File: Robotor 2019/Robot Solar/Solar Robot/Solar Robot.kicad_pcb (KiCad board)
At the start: 2 copper layers, 100.3 x 81.3 mm, 43 parts, among them J1 Conn_01x02, J2 Conn_01x06_Male, M1 Motor_DC, M2 Motor_DC, SW1 SW_DIP_x01, SW2 SW_Push, SW3 SW_Push, U1 ATmega328-PU, U2 ITR8307, U3 ITR8307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

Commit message: Solar robot final circuit board (hopefully)
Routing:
- net Net-(R4-Pad2): track 15.7 -> 18.7 mm
- net Net-(R10-Pad2): track 16.3 -> 18.8 mm
- net GND: vias 4 -> 0

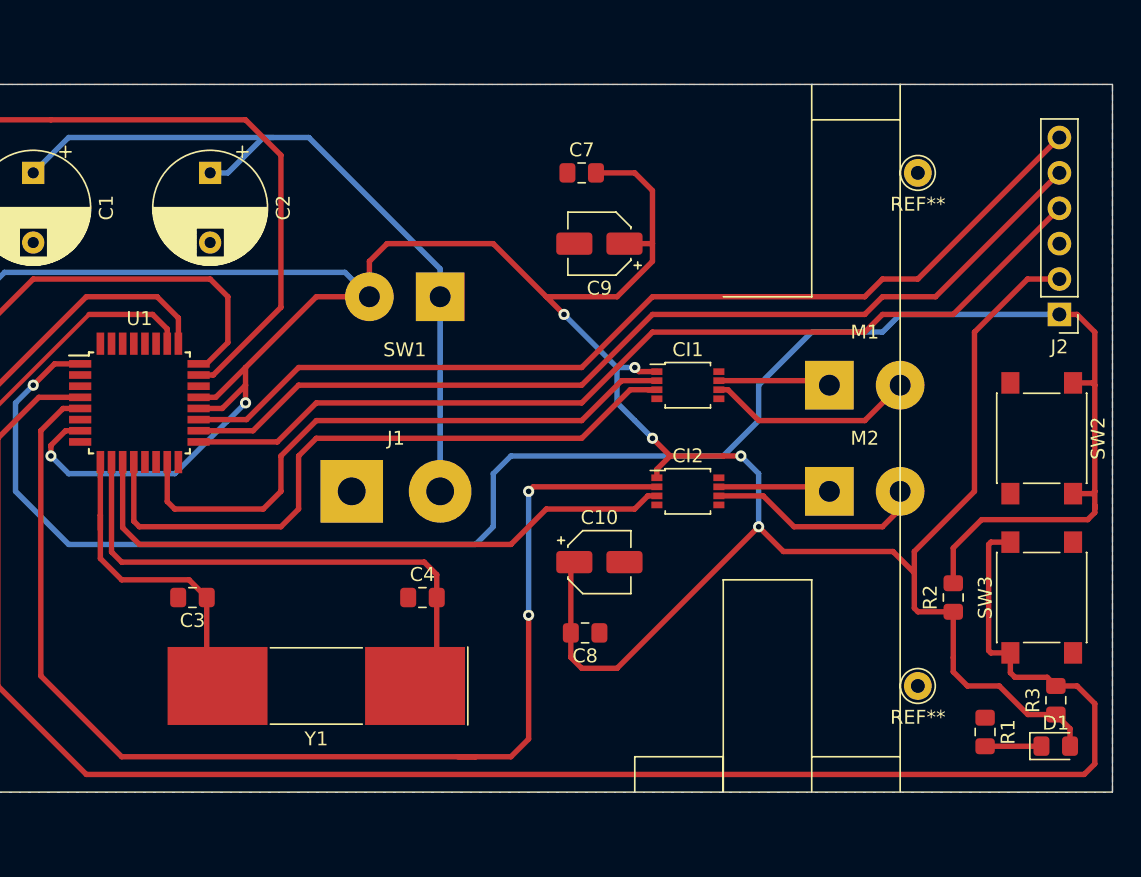
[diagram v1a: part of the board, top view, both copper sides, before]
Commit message: Final solar robot pcb schematic (added mounting holes for motors and changed clearance on existing through-holes) Added all-red pdf printer file.
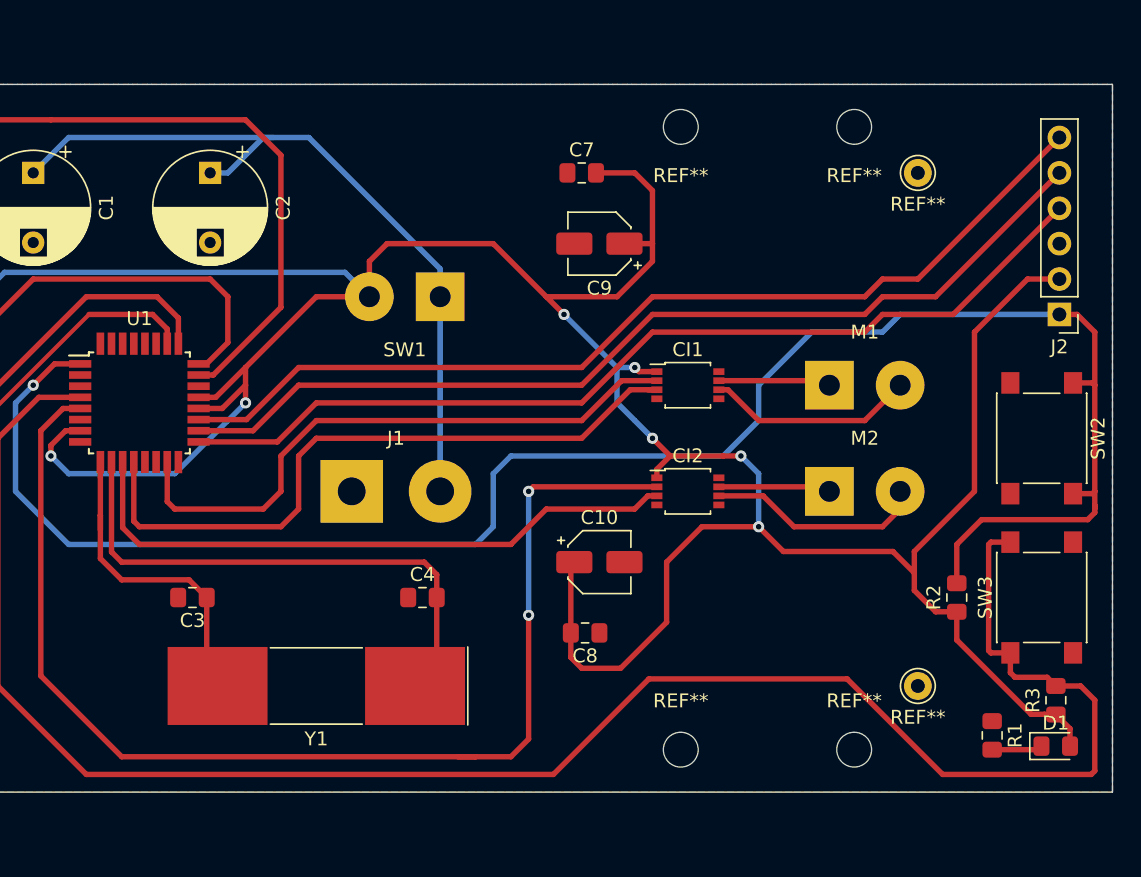
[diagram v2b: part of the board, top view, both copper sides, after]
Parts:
- added REF**: MountingHole_2.5mm, MountingHole:MountingHole_2.5mm, F.Cu at (112.5, 72.9)
- added REF**: MountingHole_2.5mm, MountingHole:MountingHole_2.5mm, F.Cu at (125.0, 72.9)
- added REF**: MountingHole_2.5mm, MountingHole:MountingHole_2.5mm, F.Cu at (112.5, 117.6)
- added REF**: MountingHole_2.5mm, MountingHole:MountingHole_2.5mm, F.Cu at (125.0, 117.6)
- moved R1 0.56 mm to (134.9, 116.6)
- moved R2 0.25 mm to (132.3, 106.7)
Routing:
- net StartBtn: track 130.2 -> 136.3 mm

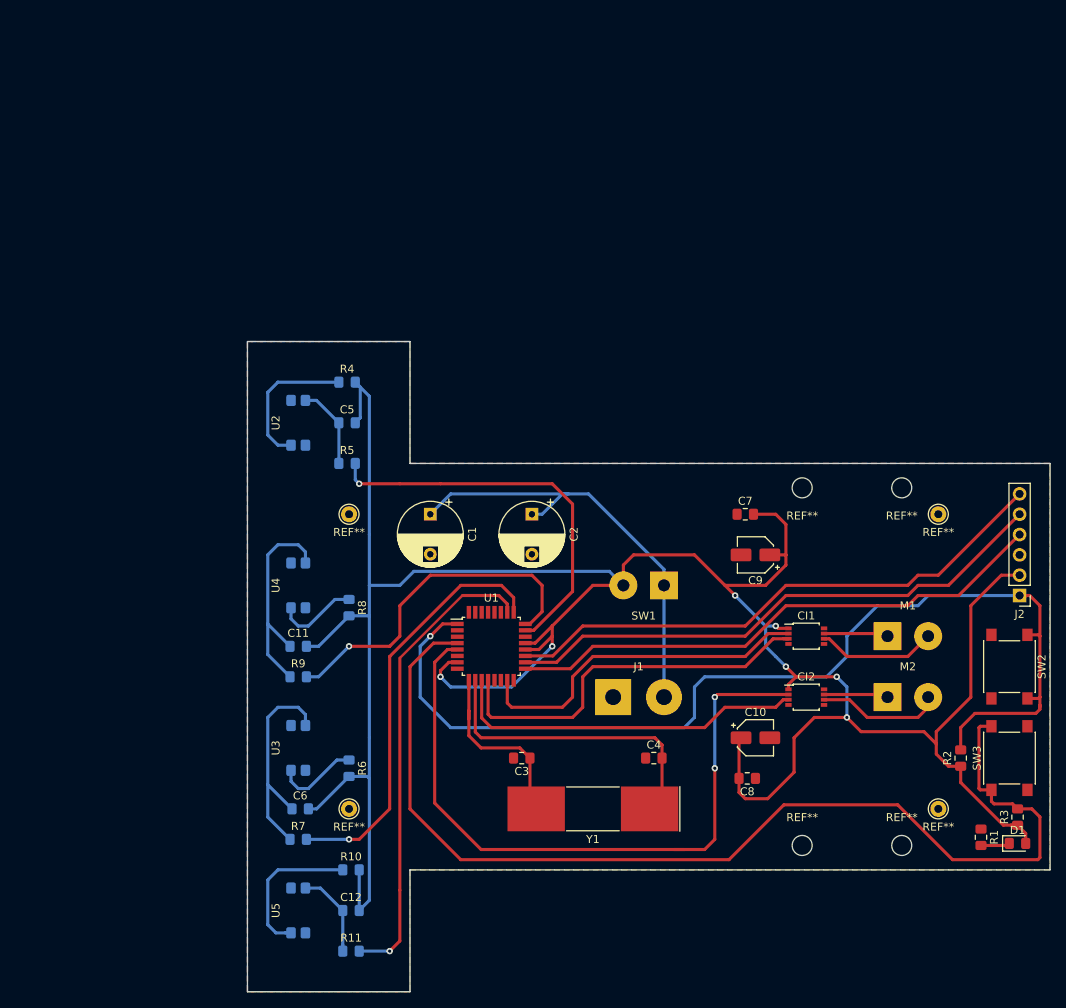
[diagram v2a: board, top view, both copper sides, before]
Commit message: Tweaked PCB track widths. Added compnent values in both eschemas. Printed Front and Back tracks and a parts list to PDF.
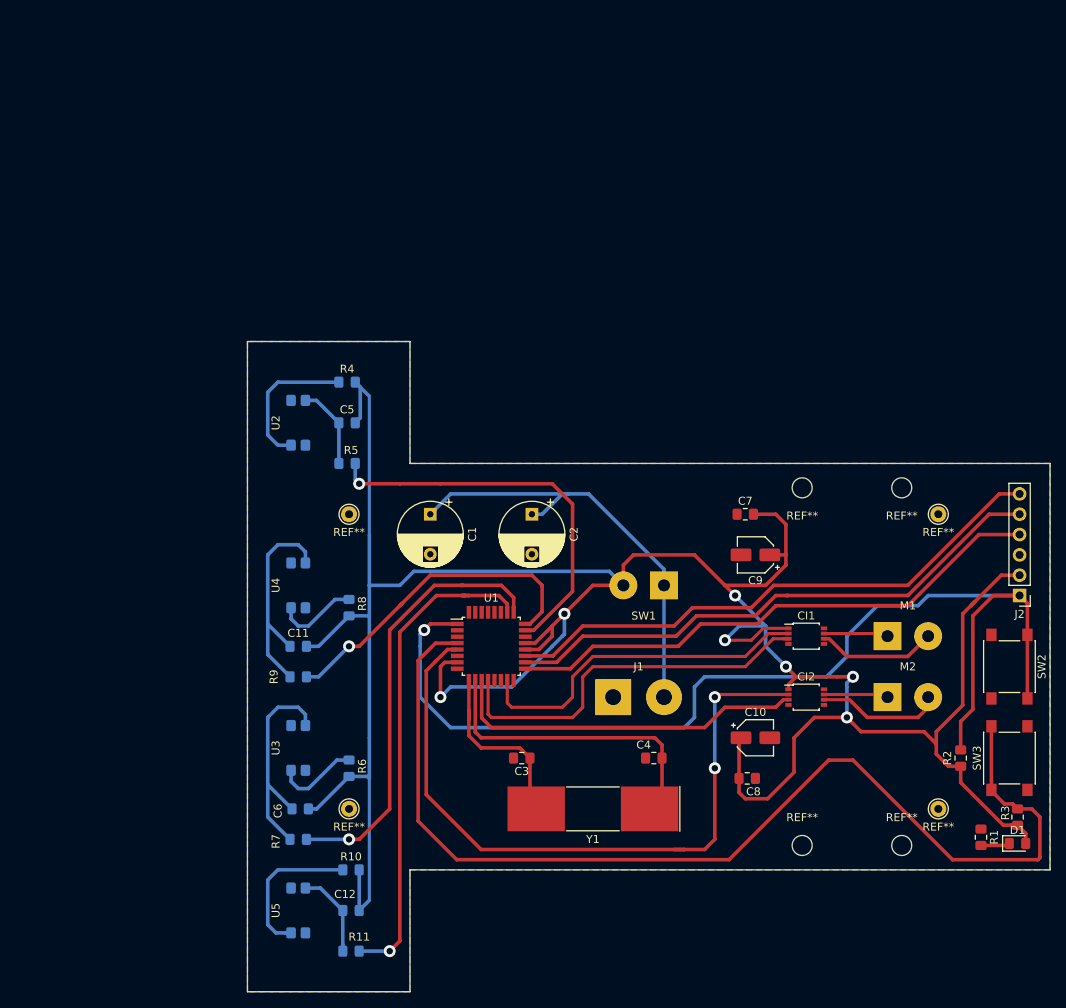
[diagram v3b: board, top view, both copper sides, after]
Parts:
- C1, C2: value CP -> 3F
- C10, C9: value CP -> 10uF
- C11, C12, C5, C6: value C -> 10nF
- C3, C4: value C -> 22p
- C7, C8: value C -> 100n
- Y1: value Crystal -> 16Mhz
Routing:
- net +5V: track 326.0 -> 346.1 mm
- net RESET: track 132.4 -> 137.7 mm
- net S4: track 59.1 -> 62.3 mm
- net S2: track 52.7 -> 54.9 mm
- net S3: track 43.5 -> 41.6 mm
- net M2IN1: track 87.4 -> 88.6 mm

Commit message: no message
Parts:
- added C13: 100n, Capacitor_SMD:C_0805_2012Metric_Pad1.15x1.40mm_HandSolder, F.Cu at (57.3, 41.8)
- added C14: 100n, Capacitor_SMD:C_0805_2012Metric_Pad1.15x1.40mm_HandSolder, F.Cu at (57.6, 36.7)
- added C15: 100n, Capacitor_SMD:C_0805_2012Metric_Pad1.15x1.40mm_HandSolder, F.Cu at (61.6, 36.7)
- U1: value ATmega328-PU -> ATmega328P-AU
- moved Y1 77.6 mm to (32.5, 57.2), turned to 90 degrees
- moved C4 73.3 mm to (37.4, 60.0), turned to 90 degrees
- moved C3 67.4 mm to (37.3, 52.5), turned to 90 degrees
- moved R7 52.4 mm to (17.4, 75.5), turned to 90 degrees
- moved C2 52.0 mm to (46.3, 35.5), turned to 0 degrees
- moved R9 50.9 mm to (19.0, 55.9)
- moved C8 49.9 mm to (76.7, 68.6)
- moved CI2 49.9 mm to (84.1, 58.4)
- moved D1 49.9 mm to (110.5, 76.7)
- moved J1 49.9 mm to (60.0, 58.4)
- moved R2 49.9 mm to (103.4, 66.0)
- moved R6 49.9 mm to (27.0, 67.3)
- moved REF** 49.9 mm to (83.6, 76.9)
- moved REF** 49.9 mm to (96.1, 76.9)
- moved REF** 49.9 mm to (27.0, 72.4)
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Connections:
- U1 pad 1: RESET -> Net-(U1-Pad1)
- U1 pad 10: Net-(C4-Pad2) -> M2IN1
- U1 pad 11: M2IN2 -> Net-(U1-Pad11)
- U1 pad 12: M1IN2 -> Net-(U1-Pad12)
- U1 pad 13: Net-(U1-Pad13) -> M1IN2
- U1 pad 14: Net-(U1-Pad14) -> M1IN1
- U1 pad 15: M1IN1 -> MOSI
- U1 pad 16: Net-(U1-Pad16) -> MISO
- U1 pad 17: MOSI -> SCK
- U1 pad 18: MISO -> +5V
- U1 pad 19: SCK -> Net-(U1-Pad19)
- U1 pad 20: +5V -> Net-(C13-Pad1)
- U1 pad 21: +5V -> GND
- U1 pad 22: GND -> Net-(U1-Pad22)
- U1 pad 29: (no net) -> RESET
- U1 pad 3: Net-(U1-Pad3) -> GND
- U1 pad 30: (no net) -> Net-(U1-Pad30)
- U1 pad 31: (no net) -> Net-(U1-Pad31)
- U1 pad 32: (no net) -> StartBtn
- U1 pad 4: StartBtn -> +5V
- U1 pad 5: M2IN1 -> GND
- U1 pad 6: Net-(U1-Pad6) -> +5V
- U1 pad 7: +5V -> Net-(C3-Pad1)
- U1 pad 8: GND -> Net-(C4-Pad2)
- U1 pad 9: Net-(C3-Pad1) -> M2IN2
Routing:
- net M2IN1: track 88.6 -> 46.1 mm, vias 2 -> 0
- net StartBtn: track 136.6 -> 162.8 mm
- net Net-(C4-Pad2): track 39.1 -> 14.5 mm
- net S4: track 62.3 -> 81.8 mm
- net Net-(C13-Pad1): track 0.00 -> 15.3 mm
- net Net-(C3-Pad1): track 23.4 -> 9.45 mm
- net S3: track 41.6 -> 54.5 mm
- net +5V: track 346.1 -> 335.6 mm, vias 7 -> 5
- net S2: track 54.9 -> 65.2 mm
- net MOSI: track 68.7 -> 76.6 mm
- net RESET: track 137.7 -> 144.8 mm
- net Net-(C1-Pad1): track 55.7 -> 48.7 mm
- net GND: track 0.00 -> 5.64 mm
- net MISO: track 69.7 -> 73.3 mm
- net M2IN2: track 45.0 -> 47.8 mm
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
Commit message: Honestly I don't even remember
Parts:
- J2: footprint Connector_PinHeader_2.54mm:PinHeader_1x06_P2.54mm_Vertical -> Connector_PinSocket_2.54mm:PinSocket_2x03_P2.54mm_Vertical
- SW2, SW3: footprint Button_Switch_SMD:SW_Push_1P1T_NO_6x6mm_H9.5mm -> Button_Switch_SMD:SW_SPST_CK_RS282G05A3
- moved J2 4.70 mm to (106.1, 45.9)
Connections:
- J2 pad 1: RESET -> GND
- J2 pad 2: +5V -> RESET
- J2 pad 3: GND -> MOSI
- J2 pad 4: MOSI -> SCK
- J2 pad 5: MISO -> +5V
- J2 pad 6: SCK -> MISO
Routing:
- net +5V: track 335.6 -> 352.7 mm
- net RESET: track 144.8 -> 131.9 mm
- net StartBtn: track 162.8 -> 153.4 mm
- net SCK: track 71.6 -> 78.6 mm
- net MOSI: track 76.6 -> 69.7 mm
- net MISO: track 73.3 -> 71.8 mm

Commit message: Slight changes to variable references and values
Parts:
- C1, C2: value 3F -> 1.5F
- R?: renamed from C5; value 10nF -> 47K
- R?: renamed from C6; value 10nF -> 47K
- R?: renamed from C11; value 10nF -> 47K
- R?: renamed from C12; value 10nF -> 47K
